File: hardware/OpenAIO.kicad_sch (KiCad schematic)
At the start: 16 parts, among them U24 AIO_outline, U25 INA186A3IDCKR

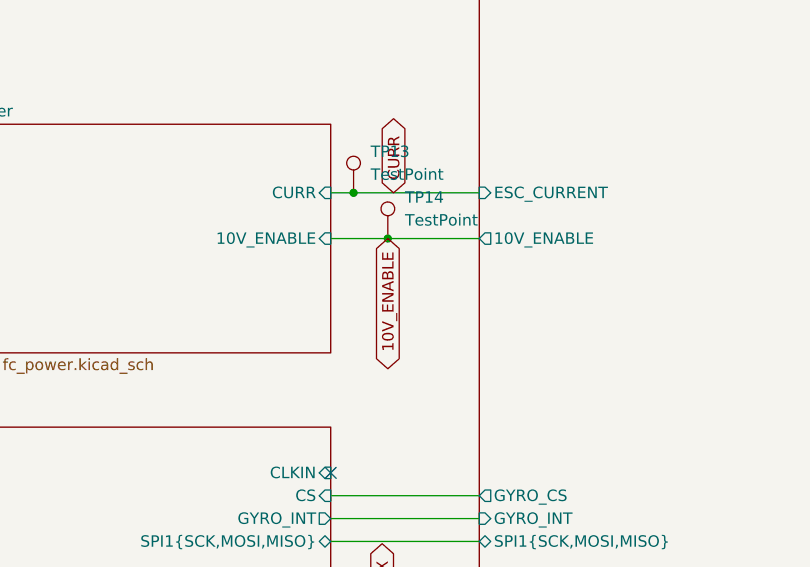
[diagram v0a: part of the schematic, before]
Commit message: Power: +10V buck always on with battery, 10V_ENABLE removed
CIRCUIT_REVIEW B1: the LMR51430 +10V buck U3 (NSG2065Q gate drive and VTX power) was enabled by RP2354A GPIO27 over LGA pad 1 with no pull, so firmware or a Betaflight PINIO could cut ESC gate drive, and on USB-only power a high GPIO27 drove EN with VIN = 0, which the LMR51430 datasheet forbids. U3 EN is now tied to +BATT exactly like U4 (datasheet: EN may be tied to VIN; no parts added). Base: U3.5 keeps its B.Cu stub and through via, re-netted to +BATT so the via lands in the +BATT planes; the In2 run, the via and the F.Cu stub to J90 pad 1 are removed. Core: the GPIO27 route to J91 pad 1 is removed. LGA pad 1 and GPIO27 are free (no-connect); the root marker TP14 of the old net is dropped. Boards saved by pcbnew 10.0.6 without zone refill; the "Tokyo" silkscreen render caches were re-rendered with a substitute font (Tokyo not installed here).

Co-Authored-By: Claude Opus 5.5 <noreply@anthropic.com>
Claude-Session: https://claude.ai/code/session_01KTp3FLjVXfXdWrkmr6af7d
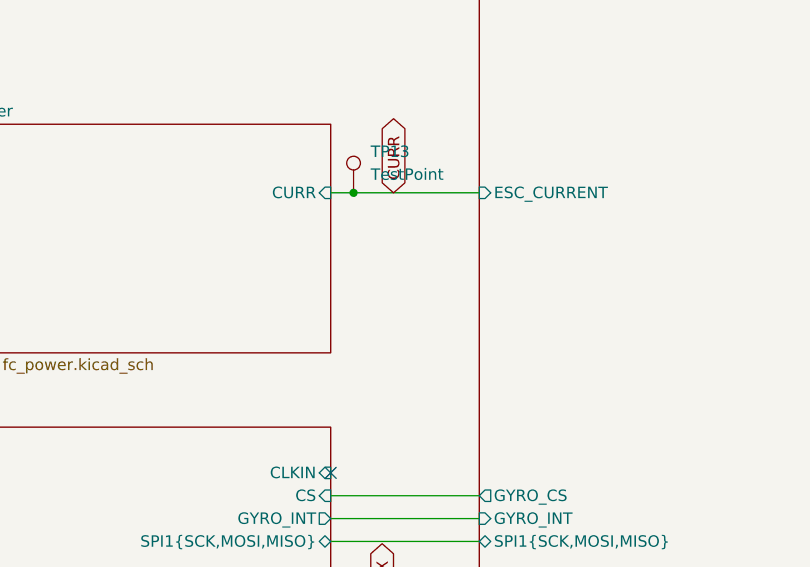
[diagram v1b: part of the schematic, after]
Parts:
- removed TP14: TestPoint, TestPoint:TestPoint_Pad_D1.0mm, symbol Connector:TestPoint
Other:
- sheet Power ports: added none; removed 10V_ENABLE
- sheet RP2354A ports: added none; removed 10V_ENABLE
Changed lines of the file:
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@@
 	(paper "A4")
 	(junction
-		(at 68.58 61.595)
-		(diameter 0)
-		(color 0 0 0 0)
-	)
-	(junction
 		(at 151.765 135.89)
 		(diameter 0)
@@
 	(wire
 		(pts
-			(xy 62.23 61.595) (xy 68.58 61.595)
-		)
-		(stroke
-			(width 0)
-			(type default)
-		)
-	)
-	(wire
-		(pts
 			(xy 211.455 75.565) (xy 216.535 75.565)
 		)
@@
 	(wire
 		(pts
-			(xy 68.58 61.595) (xy 78.74 61.595)
-		)
-		(stroke
-			(width 0)
-			(type default)
-		)
-	)
-	(wire
-		(pts
 			(xy 64.77 56.515) (xy 78.74 56.515)
 		)
@@
 		)
 	)
-	(global_label "10V_ENABLE"
-		(shape bidirectional)
-		(at 68.58 61.595 270)
-		(effects
-			(font
-				(size 1.27 1.27)
-			)
-			(justify right)
-		)
-		(property "Intersheetrefs" "${INTERSHEET_REFS}"
-			(at 68.58 61.595 0)
-			(hide yes)
-			(show_name no)
-			(do_not_autoplace no)
-			(effects
-				(font
-					(size 1.27 1.27)
-				)
-			)
-		)
-	)
 	(global_label "MOTOR2"
 		(shape bidirectional)
@@
 	)
 	(symbol
-		(lib_id "Connector:TestPoint")
-		(at 68.58 61.595 0)
-		(unit 1)
-		(body_style 1)
-		(exclude_from_sim no)
-		(in_bom no)
-		(on_board no)
-		(in_pos_files yes)
-		(dnp no)
-		(fields_autoplaced yes)
-		(property "Reference" "TP14"
-			(at 70.485 57.0229 0)
-			(show_name no)
-			(do_not_autoplace no)
-			(effects
-				(font
-					(size 1.27 1.27)
-				)
-				(justify left)
-			)
-		)
-		(property "Value" "TestPoint"
-			(at 70.485 59.5629 0)
-			(show_name no)
-			(do_not_autoplace no)
-			(effects
-				(font
-					(size 1.27 1.27)
-				)
-				(justify left)
-			)
-		)
-		(property "Footprint" "TestPoint:TestPoint_Pad_D1.0mm"
-			(at 73.66 61.595 0)
-			(hide yes)
-			(show_name no)
-			(do_not_autoplace no)
-			(effects
-				(font
-					(size 1.27 1.27)
-				)
-			)
-		)
-		(property "Datasheet" ""
-			(at 73.66 61.595 0)
-			(hide yes)
-			(show_name no)
-			(do_not_autoplace no)
-			(effects
-				(font
-					(size 1.27 1.27)
-				)
-			)
-		)
-		(property "Description" "test point"
-			(at 68.58 61.595 0)
-			(hide yes)
-			(show_name no)
-			(do_not_autoplace no)
-			(effects
-				(font
-					(size 1.27 1.27)
-				)
-			)
-		)
-		(pin "1"
-		)
-		(instances
-			(project "OpenAIO-Base"
-				(path "/fb88b6f9-ee39-4640-a9d4-04a17ceeac64"
-					(reference "TP14")
-					(unit 1)
-				)
-			)
-		)
-	)
-	(symbol
 		(lib_id "power:GND")
 		(at 236.22 94.615 0)
@@
 			)
 		)
-		(pin "10V_ENABLE" output
-			(at 78.74 61.595 180)
-			(effects
-				(font
-					(size 1.27 1.27)
-				)
-				(justify left)
-			)
-		)
 		(pin "BUZZER-" output
 			(at 145.415 33.02 0)
@@
 			)
 		)
-		(pin "10V_ENABLE" input
-			(at 62.23 61.595 0)
-			(effects
-				(font
-					(size 1.27 1.27)
-				)
-				(justify right)
-			)
-		)
 		(pin "CURR" input
 			(at 62.23 56.515 0)
@@
 		)
 	)
-	(embedded_fonts no)
 )

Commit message: Owner rules: no component silk, pad labels and values, no wordmark text, MPN + maker on every BOM line
The owner rules adopted in PLAN.md (pcb-agent-commons, 2026-10-06), applied
where they are local edits:

- No component silkscreen. J91's reference was the only visible one (Core
  B.Silkscreen, under the LGA) and is hidden. Footprint silk graphics removed
  per instance: Base 234, Core 72. Kept: connector outlines and pin-1 marks
  (USB1, U12 SH-6, Card1, JP1) and the LGA pin-1 marks (J90, J91). Base
  lib_footprint_mismatch warnings 31 -> 40 as a result.
- Solder-pad labels: Core J53 (GND) had none, now "gnd" in the style of J52's
  label. The SH-6 per-pin labels ("10v gnd T0", "R0 gnd R1") become the port
  name "DJI" (connectors: name and pin-1 mark only). Core J48-J51 have no room:
  0.5 mm to J44 above, 0.93 mm to the board edge below. CIRCUIT_REVIEW 8.3
  moves them off the LGA in R2, so their labels go with that move.
- Pad values: all 40 solder-pad symbols said "5V". Each now carries its
  function (5V, GND, LED, BUZ+/BUZ-, 10V, 4V5, CAM, VTX, SCL, SDA, TX0/RX0,
  TX1/RX1, PIO_TX0/PIO_RX0; off-board J19 ADC2, J22 GND, J46/J47 NC).
- No "Drone" text: the "OpenDrone" wordmark on Core F.Silkscreen (9 filled
  polygons in two groups) is removed; a TODO for the incutec wordmark from the
  brand repo sits on User.Comments (not fabricated). No other such text on any
  copper, mask or silk layer of either board.
- BOM: lines missing manufacturer or MPN 41 -> 1. MPNs come from
  PARTS-USED.md by LCSC number. Manufacturers come from the catalogue symbol,
  this design's spelling for the same MPN family, or the committed datasheet
  (NSIC, Sofng, Jiangsu Changjing, Hirose). Still open: Rsense2
  ASR-S-3-0.2F (C695806), whose manufacturer nothing in the catalogue states.
  U24 (board outline) and TP9 (BOOT solder pad) are not parts: excluded from
  BOM and position files.
- 0201 default / minimal capacitance: respected in the circuit commit (C26
  stays 0201; no belt-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
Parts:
- C104: Manufacturer (none) -> Murata Electronics
- U24: now left out of the parts list
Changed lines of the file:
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@@
 			)
 		)
-		(property "Manufacturer" ""
+		(property "Manufacturer" "Murata Electronics"
 			(at -58.42 -3.81 0)
 			(hide yes)
@@
 		(body_style 1)
 		(exclude_from_sim no)
-		(in_bom yes)
+		(in_bom no)
 		(on_board yes)
-		(in_pos_files yes)
+		(in_pos_files no)
 		(dnp no)
 		(fields_autoplaced yes)

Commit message: Schematic readability: TP texts, C19/C107, C26, title blocks (FB5 item 6, V9-V11/M6)
- TestPoint values ('TestPoint') hidden on all sheets: the stacked TP16/TP17
  (root), TP24/TP25 and TP18/TP19/TP26/TP27 (RP2354A) texts no longer overlap.
- C19 reference/value moved left of the part (no longer printed over C107).
- C26 Description field hidden.
- Title blocks: rev r2, date 2026-10 (title added where missing) on the root,
  RP2354A, Power, IMU, OSD, Pads, ESC channel and Core interface sheets.
Edited with kicad-skip, re-saved with `kicad-cli sch upgrade --force` so the
diff stays minimal. Not done: rx_esp32c3_sx1281 and fc_blackbox title blocks
(they carry other projects' instances, OpenRX-Lite / BLACKBOX, and the headless
re-save renumbers their references); TP10 outside the frame (moving it would
detach its wire); N4 SPI0 label lift (label position is the connection point);
M7 net naming (+4v5 / +3.3V vs +3V3) left as is, it touches the LGA spec.
ERC 31 errors (unchanged).

Co-Authored-By: Claude Opus 5.5 <noreply@anthropic.com>
Claude-Session: https://claude.ai/code/session_01KTp3FLjVXfXdWrkmr6af7d
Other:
- title: (none) -> OpenAIO (Core + Base)
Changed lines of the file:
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@@
 	(generator_version "10.0")
 	(paper "A4")
+	(title_block
+		(title "OpenAIO (Core + Base)")
+		(date "2026-10")
+		(rev "r2")
+	)
 	(junction
 		(at 151.765 135.89)
@@
 		(property "Value" "TestPoint"
 			(at 153.5882 105.9179 0)
+			(hide yes)
 			(show_name no)
 			(do_not_autoplace no)
@@
 		(property "Value" "TestPoint"
 			(at 153.67 91.9479 0)
+			(hide yes)
 			(show_name no)
 			(do_not_autoplace no)
@@
 		(property "Value" "TestPoint"
 			(at 153.035 22.0979 0)
+			(hide yes)
 			(show_name no)
 			(do_not_autoplace no)
@@
 		(property "Value" "TestPoint"
 			(at 154.305 46.8629 0)
+			(hide yes)
 			(show_name no)
 			(do_not_autoplace no)
@@
 		(property "Value" "TestPoint"
 			(at 74.295 108.4579 0)
+			(hide yes)
 			(show_name no)
 			(do_not_autoplace no)
@@
 		(property "Value" "TestPoint"
 			(at 72.39 102.1079 0)
+			(hide yes)
 			(show_name no)
 			(do_not_autoplace no)
@@
 		(property "Value" "TestPoint"
 			(at 153.67 133.8579 0)
+			(hide yes)
 			(show_name no)
 			(do_not_autoplace no)
@@
 		(property "Value" "TestPoint"
 			(at 66.675 54.4829 0)
+			(hide yes)
 			(show_name no)
 			(do_not_autoplace no)
@@
 		(property "Value" "TestPoint"
 			(at 152.4 30.9879 0)
+			(hide yes)
 			(show_name no)
 			(do_not_autoplace no)
@@
 		(property "Value" "TestPoint"
 			(at 154.305 44.3229 0)
+			(hide yes)
 			(show_name no)
 			(do_not_autoplace no)
@@
 		(property "Value" "TestPoint"
 			(at 153.67 119.8879 0)
+			(hide yes)
 			(show_name no)
 			(do_not_autoplace no)

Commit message: One board: merge Base and Core onto the OpenAIO-Whoop 8L HDI stackup
- hardware/OpenAIO.kicad_pcb: the routed Base and Core layouts of 8fa8d7b
  side by side in one board, all routing kept (Core promoted to 8 layers
  before the append so no Base layer was dropped). J90/J91 LGA deleted;
  their 46 nets are now direct links (51 unconnected, listed in
  research/ROUTING.md). Stackup and board setup from OpenAIO-Whoop:
  8L HDI 1+6+1, 0.997 mm, 1 oz all layers, microvia 0.25/0.10,
  buried 0.33/0.15. Base DRC severities and exclusions kept.
- hardware/OpenAIO.kicad_dru: canonical block, Whoop HDI via rules,
  Base/Core rules that still apply; LGA, 2 oz and 1.6 mm via rules gone.
- Schematic: core_interface sheet removed; DPS368 baro U28 on I2C0;
  review fixes (U3 HF cap C116, RP2354 caps C117/C118, buzzer flyback D10,
  SD card on +3.3V, D9 on +4v5, FLASH_CS -> SD_CS, PWR_FLAGs, U7 pin
  names, ESC cap pin types, L4 LCSC). ERC 32 -> 0 errors.
- Libraries project-local: every footprint, 3D model and symbol in lib;
  OPENDRONE_LIB aliases removed from the lib tables.
- Two-board projects, multiboard config and LGA tools removed; Whoop
  board tools added in hardware/tools.
- Docs: README, AGENTS.md, research/ROUTING.md (hand-over),
  SCHEMATIC-REVIEW-2026-10-15.md, Betaflight target baro.

DRC: 38 errors (25 dangling LGA escape vias, 13 Core leftovers listed),
51 unconnected (the Base-Core links), 0 net or value parity issues.

Co-Authored-By: Claude Opus 5.5 <noreply@anthropic.com>
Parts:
- C104: footprint Capacitor_SMD:C_0201_0603Metric -> lib:C_0201_0603Metric; symbol ESCLibrary:GRM033R61C104KE84D -> lib:GRM033R61C104KE84D
- Rsense2: footprint Resistor_SMD:R_2512_6332Metric -> lib:R_2512_6332Metric
- TP12, TP13, TP15, TP16, TP17, TP20, TP21, TP22, TP23, TP29, TP41: footprint TestPoint:TestPoint_Pad_D1.0mm -> lib:TestPoint_Pad_D1.0mm
- U24: footprint OpenDrone:AIO_outline -> lib:AIO_outline
- U25: footprint 4in1ESC:SOT-363_SC-70-6 -> lib:SOT-363_SC-70-6; symbol components:INA186A3IDCKR -> lib:INA186A3IDCKR
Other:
- removed sheet Core_Interface
- sheet Blackbox ports: added SD_CS; removed FLASH_CS
- sheet Power ports: added none; removed CURR
- sheet RP2354A ports: added SD_CS; removed FLASH_CS
- title: OpenAIO (Core + Base) -> OpenAIO

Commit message: One board from the owner's 2026-08-22 Base and Core, BMP580 baro (#26)
The board is rebuilt from d81e559 (the hand-routed Base recovered from KiCad
local history and the hand-routed Core of 1fe3d21) plus the always-on +10V of
9aba717, instead of the agent-reworked 8fa8d7b. Both layouts sit side by side
in hardware/OpenAIO.kicad_pcb with all routing kept (2513 tracks, 1577 vias),
on the OpenAIO-Whoop 8L HDI stackup.

- Schematic: Core_Interface (J90/J91 LGA) removed; U26 BMP580 + C107/C108 on
  I2C0 at 0x47 (Betaflight BMP5xx default). Netlist otherwise identical to
  9aba717; ERC 31 errors, the 9aba717 baseline.
- Board: Base netclasses and severities; rule area "Core layout" keeps the
  Core's 0.09 line standard. DRC: 3 errors (USB1 peg), 37 unconnected (links).
- lib.pretty footprints replaced by the board instances; BMP580 imported with
  easyeda2kicad (LCSC C22391138).
- Not carried from 8fa8d7b: TXU0101 LED-strip buffer, +3V3_ESC, SWD pads,
  DFM edits; firmware ISSUES I2/I3 reopened.
- Docs: README pinout re-measured, AGENTS.md, research/ROUTING.md, Betaflight
  target USE_BARO_BMP580.

Co-authored-by: Stan <stan@openaio.local>
Co-authored-by: Claude Opus 5.5 <noreply@anthropic.com>
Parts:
- C104: Manufacturer Murata Electronics -> (none)
- U24: now in the parts list
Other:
- sheet Blackbox ports: added FLASH_CS; removed SD_CS
- sheet Power ports: added CURR; removed none
- sheet RP2354A ports: added FLASH_CS; removed SD_CS
- title: OpenAIO -> (none)
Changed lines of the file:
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@@
 	(generator_version "10.0")
 	(paper "A4")
-	(title_block
-		(title "OpenAIO")
-		(date "2026-10")
-		(rev "r2")
-	)
 	(junction
 		(at 151.765 135.89)
@@
 		)
 	)
-	(bus
+	(wire
 		(pts
 			(xy 145.415 35.56) (xy 170.815 35.56)
@@
 		)
 	)
-	(bus
+	(wire
 		(pts
 			(xy 62.23 95.25) (xy 78.74 95.25)
@@
 		)
 	)
-	(bus
+	(wire
 		(pts
 			(xy 145.415 62.865) (xy 170.815 62.865)
@@
 	(wire
 		(pts
+			(xy 62.23 56.515) (xy 64.77 56.515)
+		)
+		(stroke
+			(width 0)
+			(type default)
+		)
+	)
+	(wire
+		(pts
 			(xy 62.23 107.95) (xy 70.485 107.95)
 		)
@@
 		)
 	)
-	(global_label "SD_CS"
+	(global_label "FLASH_CS"
 		(shape bidirectional)
 		(at 167.355 60.325 90)
@@
 		(property "Value" "TestPoint"
 			(at 153.5882 105.9179 0)
-			(hide yes)
 			(show_name no)
 			(do_not_autoplace no)
@@
 		(property "Value" "TestPoint"
 			(at 153.67 91.9479 0)
-			(hide yes)
 			(show_name no)
 			(do_not_autoplace no)
@@
 	)
 	(symbol
-		(lib_id "power:PWR_FLAG")
-		(at 236.22 112.395 0)
-		(unit 1)
-		(body_style 1)
-		(exclude_from_sim no)
-		(in_bom yes)
-		(on_board yes)
-		(in_pos_files yes)
-		(dnp no)
-		(property "Reference" "#FLG0943"
-			(at 236.22 110.495 0)
-			(hide yes)
-			(show_name no)
-			(do_not_autoplace no)
-			(effects
-				(font
-					(size 1.27 1.27)
-				)
-			)
-		)
-		(property "Value" "PWR_FLAG"
-			(at 236.22 108.585 0)
-			(show_name no)
-			(do_not_autoplace no)
-			(effects
-				(font
-					(size 1.27 1.27)
-				)
-			)
-		)
-		(property "Footprint" ""
-			(at 236.22 112.395 0)
-			(hide yes)
-			(show_name no)
-			(do_not_autoplace no)
-			(effects
-				(font
-					(size 1.27 1.27)
-				)
-			)
-		)
-		(property "Datasheet" ""
-			(at 236.22 112.395 0)
-			(hide yes)
-			(show_name no)
-			(do_not_autoplace no)
-			(effects
-				(font
-					(size 1.27 1.27)
-				)
-			)
-		)
-		(property "Description" ""
-			(at 236.22 112.395 0)
-			(show_name no)
-			(do_not_autoplace no)
-			(effects
-				(font
-					(size 1.27 1.27)
-				)
-			)
-		)
-		(pin "1"
-		)
-		(instances
-			(project "OpenAIO"
-				(path "/fb88b6f9-ee39-4640-a9d4-04a17ceeac64"
-					(reference "#FLG0943")
-					(unit 1)
-				)
-			)
-		)
-	)
-	(symbol
 		(lib_id "lib:INA186A3IDCKR")
 		(at 265.43 137.16 0)
@@
 		(property "Value" "TestPoint"
 			(at 153.035 22.0979 0)
-			(hide yes)
 			(show_name no)
 			(do_not_autoplace no)
@@
 		(property "Value" "TestPoint"
 			(at 154.305 46.8629 0)
-			(hide yes)
 			(show_name no)
 			(do_not_autoplace no)
@@
 		(property "Value" "TestPoint"
 			(at 74.295 108.4579 0)
-			(hide yes)
 			(show_name no)
 			(do_not_autoplace no)
@@
 			)
 		)
-		(property "Manufacturer" "Murata Electronics"
+		(property "Manufacturer" ""
 			(at -58.42 -3.81 0)
 			(hide yes)
@@
 		(property "Value" "TestPoint"
 			(at 72.39 102.1079 0)
-			(hide yes)
 			(show_name no)
 			(do_not_autoplace no)
@@
 		(body_style 1)
 		(exclude_from_sim no)
-		(in_bom no)
+		(in_bom yes)
 		(on_board yes)
-		(in_pos_files no)
+		(in_pos_files yes)
 		(dnp no)
 		(fields_autoplaced yes)
@@
 		(property "Value" "TestPoint"
 			(at 153.67 133.8579 0)
-			(hide yes)
 			(show_name no)
 			(do_not_autoplace no)
@@
 		(property "Value" "TestPoint"
 			(at 66.675 54.4829 0)
-			(hide yes)
 			(show_name no)
 			(do_not_autoplace no)
@@
 		(property "Value" "TestPoint"
 			(at 152.4 30.9879 0)
-			(hide yes)
 			(show_name no)
 			(do_not_autoplace no)
@@
 		(property "Value" "TestPoint"
 			(at 154.305 44.3229 0)
-			(hide yes)
 			(show_name no)
 			(do_not_autoplace no)
@@
 		(property "Value" "TestPoint"
 			(at 153.67 119.8879 0)
-			(hide yes)
 			(show_name no)
 			(do_not_autoplace no)
@@
 			)
 		)
-		(pin "SD_CS" output
+		(pin "FLASH_CS" output
 			(at 145.415 60.325 0)
 			(effects
@@
 			)
 		)
-		(pin "SD_CS" input
+		(pin "FLASH_CS" input
 			(at 170.815 60.325 180)
 			(effects
@@
 			)
 		)
+		(pin "CURR" input
+			(at 62.23 56.515 0)
+			(effects
+				(font
+					(size 1.27 1.27)
+				)
+				(justify right)
+			)
+		)

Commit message: Library: every symbol, footprint and 3D model project-local (#28)
* Owner: board cleanup, Core placed on the board

Co-Authored-By: Claude Opus 5.5 <noreply@anthropic.com>

* Library: every symbol, footprint and 3D model project-local

- 3D models: 275 board model paths and 28 lib.pretty footprints pointed at
  KiCad's stock install or at ${OPENDRONE_LIB} (which this machine's KiCad sets
  to a path that does not exist, so 9 models were missing). All now resolve to
  ${KIPRJMOD}/lib.3dshapes; the three missing ones come from the repo's
  KiCad-Library submodule. .wrl replaced by the .step sibling where one exists.
- Symbols: the 14 stock symbols (Device, power, Connector, Connector_Generic,
  MCU_Espressif) copied into lib.kicad_sym from the schematic's own cache and
  relinked as lib:. Four lib symbols refreshed from the schematic (they still
  held the 8fa8d7b copies).
- Pruned: 11 unused footprints, 7 unused symbols, unreferenced model files.
- tools/localise_models.py and tools/localise_symbols.py keep it that way.
- Checks: board diff is model lines only; netlist identical; ERC 31 errors as
  before, lib_symbol_mismatch 9 -> 0.

Co-Authored-By: Claude Opus 5.5 <noreply@anthropic.com>

---------

Co-authored-by: Stan <stan@openaio.local>
Co-authored-by: Claude Opus 5.5 <noreply@anthropic.com>
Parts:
- Rsense2: symbol Device:R -> lib:R
- TP12, TP13, TP15, TP16, TP17, TP20, TP21, TP22, TP23, TP29, TP41: symbol Connector:TestPoint -> lib:TestPoint
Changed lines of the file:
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@@
 	)
 	(symbol
-		(lib_id "Device:R")
+		(lib_id "lib:R")
 		(at 236.22 129.54 0)
 		(unit 1)
@@
 	)
 	(symbol
-		(lib_id "power:+BATT")
+		(lib_id "lib:+BATT")
 		(at 223.52 135.89 0)
 		(unit 1)
@@
 	)
 	(symbol
-		(lib_id "Connector:TestPoint")
+		(lib_id "lib:TestPoint")
 		(at 151.6832 107.95 0)
 		(unit 1)
@@
 	)
 	(symbol
-		(lib_id "Connector:TestPoint")
+		(lib_id "lib:TestPoint")
 		(at 151.765 93.98 0)
 		(unit 1)
@@
 	)
 	(symbol
-		(lib_id "power:GND")
+		(lib_id "lib:GND")
 		(at 257.81 128.27 0)
 		(unit 1)
@@
 	)
 	(symbol
-		(lib_id "Connector:TestPoint")
+		(lib_id "lib:TestPoint")
 		(at 151.13 24.13 0)
 		(unit 1)
@@
 	)
 	(symbol
-		(lib_id "Connector:TestPoint")
+		(lib_id "lib:TestPoint")
 		(at 152.4 48.895 0)
 		(unit 1)
@@
 	)
 	(symbol
-		(lib_id "Connector:TestPoint")
+		(lib_id "lib:TestPoint")
 		(at 72.39 110.49 0)
 		(unit 1)
@@
 	)
 	(symbol
-		(lib_id "Connector:TestPoint")
+		(lib_id "lib:TestPoint")
 		(at 70.485 104.14 0)
 		(unit 1)
@@
 	)
 	(symbol
-		(lib_id "power:+3V3")
+		(lib_id "lib:+3V3")
 		(at 265.43 119.38 0)
 		(unit 1)
@@
 	)
 	(symbol
-		(lib_id "Connector:TestPoint")
+		(lib_id "lib:TestPoint")
 		(at 151.765 135.89 0)
 		(unit 1)
@@
 	)
 	(symbol
-		(lib_id "power:GND")
+		(lib_id "lib:GND")
 		(at 265.43 147.32 0)
 		(unit 1)
@@
 	)
 	(symbol
-		(lib_id "Connector:TestPoint")
+		(lib_id "lib:TestPoint")
 		(at 64.77 56.515 0)
 		(unit 1)
@@
 	)
 	(symbol
-		(lib_id "power:GND")
+		(lib_id "lib:GND")
 		(at 241.3 112.395 0)
 		(unit 1)
@@
 	)
 	(symbol
-		(lib_id "power:GND")
+		(lib_id "lib:GND")
 		(at 236.22 94.615 0)
 		(unit 1)
@@
 	)
 	(symbol
-		(lib_id "Connector:TestPoint")
+		(lib_id "lib:TestPoint")
 		(at 150.495 33.02 0)
 		(unit 1)
@@
 	)
 	(symbol
-		(lib_id "Connector:TestPoint")
+		(lib_id "lib:TestPoint")
 		(at 152.4 46.355 0)
 		(unit 1)
@@
 	)
 	(symbol
-		(lib_id "power:GND")
+		(lib_id "lib:GND")
 		(at 275.59 132.08 90)
 		(unit 1)
@@
 	)
 	(symbol
-		(lib_id "Connector:TestPoint")
+		(lib_id "lib:TestPoint")
 		(at 151.765 121.92 0)
 		(unit 1)
